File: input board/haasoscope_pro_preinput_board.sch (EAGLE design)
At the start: 20 parts, among them J1 MOLEX_BNC_73100-0105, J4 8pin, K1 AQY21SOP

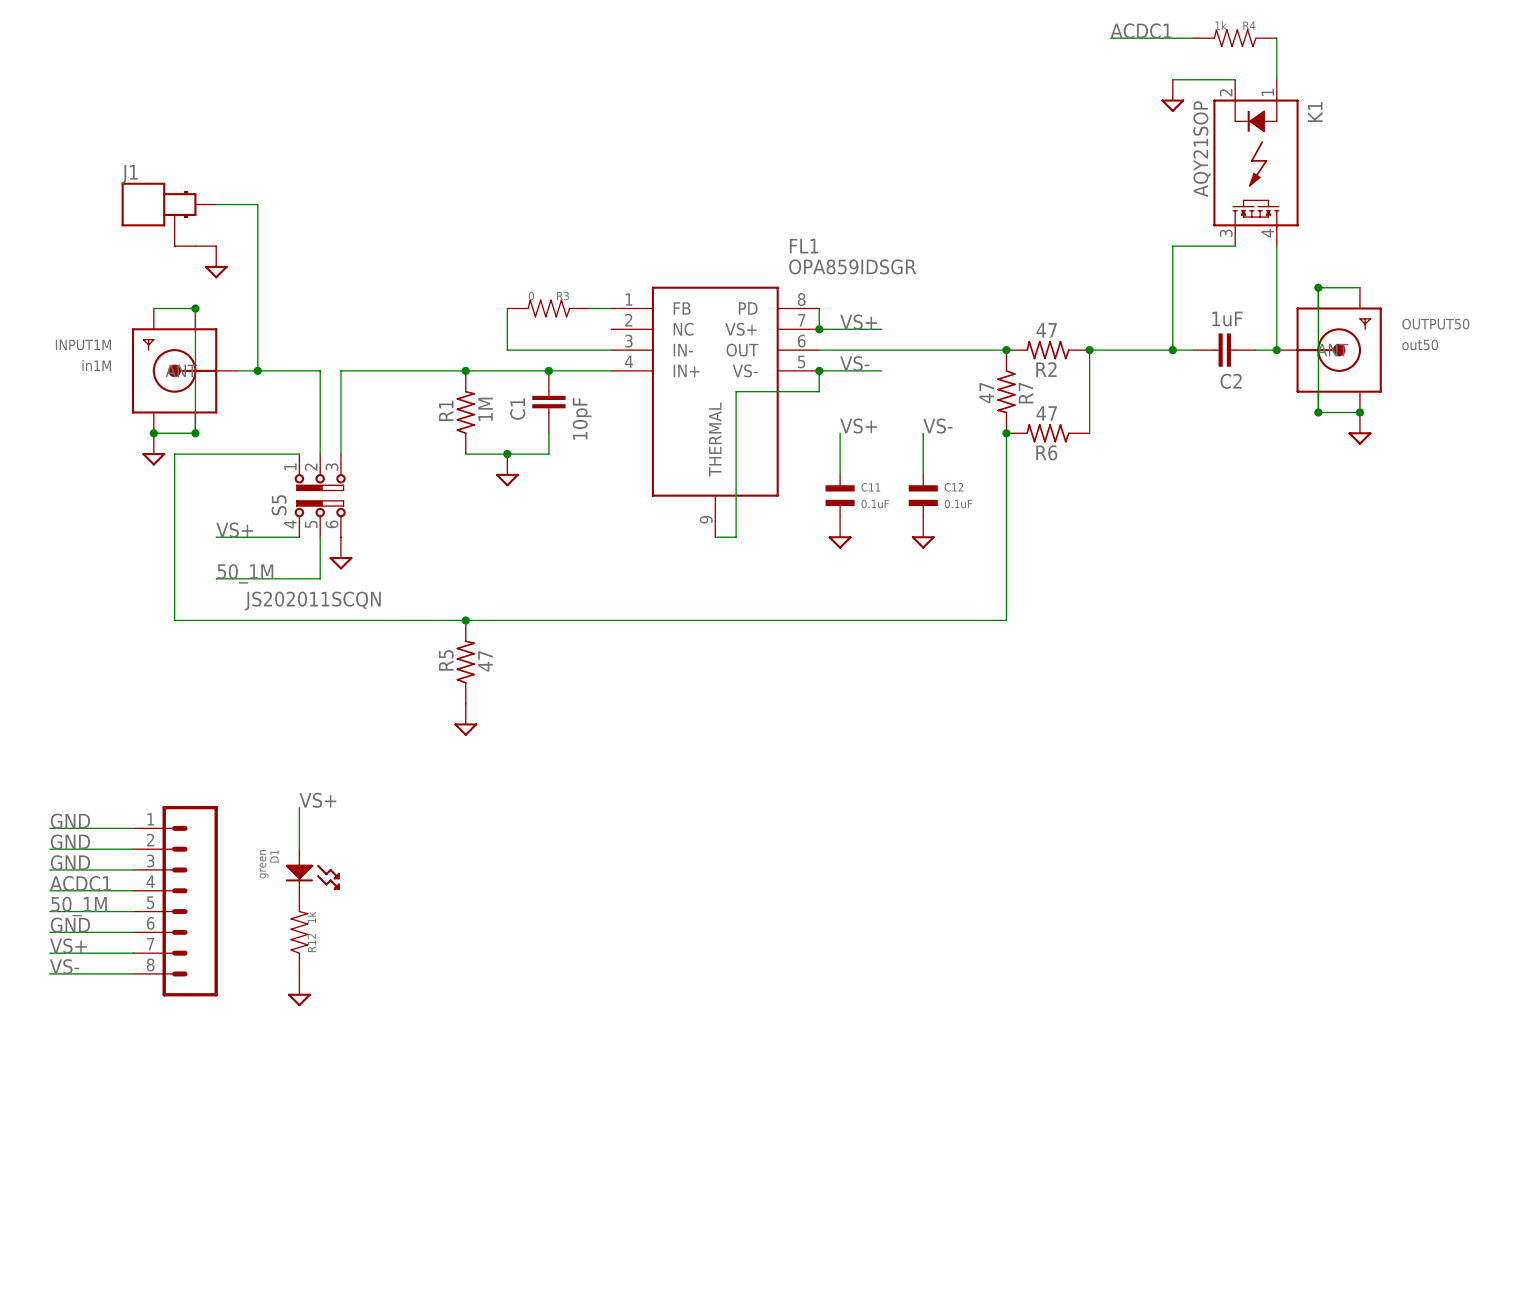
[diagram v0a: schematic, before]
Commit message: use rf relay instead of switch
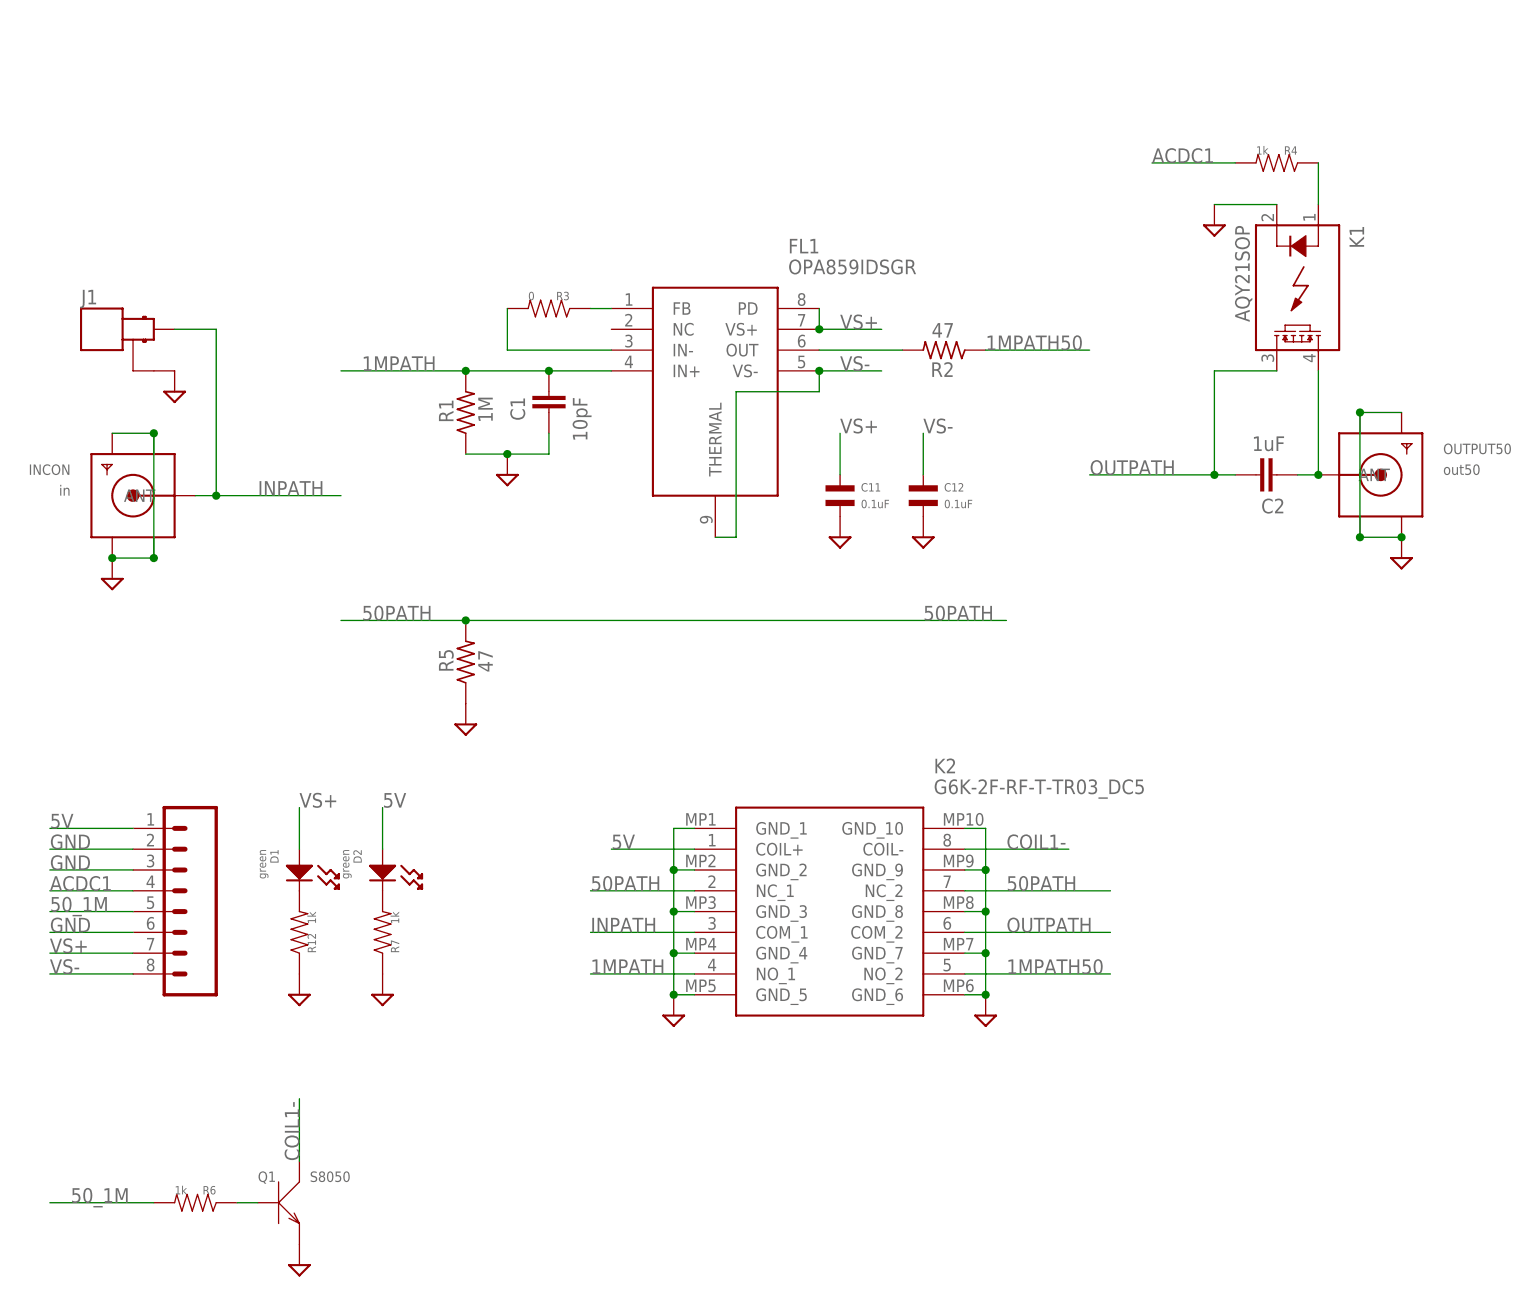
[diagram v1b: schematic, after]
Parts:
- removed INPUT1M: in1M, adafruit:SMACONNECTOR_EDGE
- removed S5: JS202011SCQN, switch-ck:JS202011SCQN
- added D2: green, MF_LEDs:LED_SINGLE-0603
- added INCON: in, adafruit:SMACONNECTOR_EDGE
- added K2: G6K-2F-RF-T-TR03_DC5, G6K-2F-RF-T-TR03_DC5:G6K-2F-RF-T-TR03_DC5
- added Q1: S8050, Seeed-Transistor:SMD-TRANSISTORS-NPN-25V-500MW-S8050(SOT-23)
- K1: LCSC (none) -> C7435105
- R6, R7: value 47 -> 1k; device resistor:R-US_R0805 -> MF_Passives:RESISTOR_0402
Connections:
- removed net N$10: C1.2, FL1.IN+, R1.2, S5.3
- removed net N$13: R5.2, R6.2, R7.2, S5.1
- removed net N$8: C2.2, K1.DS2, R2.1, R6.1
- new net 1MPATH: C1.2, FL1.IN+, K2.NO_1, R1.2
- new net 1MPATH50: K2.NO_2, R2.1
- new net 50PATH: K2.NC_1, K2.NC_2, R5.2
- new net 5V: D2.ANODE, J4.1, K2.COIL+
- new net COIL1-: K2.COIL-, Q1.C
- new net INPATH: INCON.ANT, J1.SIGNAL, K2.COM_1
- new net N$7: D2.CATHODE, R7.P$2
- new net OUTPATH: C2.2, K1.DS2, K2.COM_2
- net 50_1M: now also R6.P$2; no longer S5.5
- net GND: now also INCON.GND1, INCON.GND2, INCON.GND3, INCON.GND4, K2.GND_1, K2.GND_10, K2.GND_2, K2.GND_3, K2.GND_4, K2.GND_5, K2.GND_6, K2.GND_7, K2.GND_8, K2.GND_9, Q1.E, R7.P$1; no longer INPUT1M.GND1, INPUT1M.GND2, INPUT1M.GND3, INPUT1M.GND4, J4.1, S5.6
- net N$4: no longer R7.1
- net N$6: now also Q1.B, R6.P$1; no longer INPUT1M.ANT, J1.SIGNAL, S5.2
- net VS+: no longer S5.4
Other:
- moved on the sheet: C2, J1, K1, OUTPUT50, R2, R4, R6, R7

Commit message: use rf relay instead of switch
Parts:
- K2: LCSC (none) -> C397195
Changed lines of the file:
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@@
 <part name="R5" library="resistor" library_urn="urn:adsk.eagle:library:348" deviceset="R-US_" device="R0805" package3d_urn="urn:adsk.eagle:package:23553/2" value="47"/>
 <part name="SUPPLY5" library="supply2" library_urn="urn:adsk.eagle:library:372" deviceset="GND" device=""/>
-<part name="K2" library="G6K-2F-RF-T-TR03_DC5" deviceset="G6K-2F-RF-T-TR03_DC5" device=""/>
+<part name="K2" library="G6K-2F-RF-T-TR03_DC5" deviceset="G6K-2F-RF-T-TR03_DC5" device="">
+<attribute name="LCSC" value="C397195"/>
+</part>
 <part name="Q1" library="Seeed-Transistor" library_urn="urn:adsk.eagle:library:477" deviceset="SMD-TRANSISTORS-NPN-25V-500MW-S8050(SOT-23)" device="" package3d_urn="urn:adsk.eagle:package:33015/1" value="S8050">
 <attribute name="LCSC" value="C7420370"/>
@@
 <attribute name="NAME" x="306.07" y="25.4" size="1.778" layer="95" align="center-left"/>
 <attribute name="VALUE" x="306.07" y="22.86" size="1.778" layer="96" align="center-left"/>
+<attribute name="LCSC" x="276.86" y="17.78" size="1.778" layer="96" display="off"/>
 </instance>
 <instance part="Q1" gate="G$1" x="226.06" y="-27.94" smashed="yes">

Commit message: add attenuator and fix relay footprint
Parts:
- removed K2: G6K-2F-RF-T-TR03_DC5, G6K-2F-RF-T-TR03_DC5:G6K-2F-RF-T-TR03_DC5
- removed OUTPUT50: out50, adafruit:SMACONNECTOR_EDGE
- removed R3: 0, MF_Passives:RESISTOR_0402
- added K3: G6K-2F-RF-DC3, G6K-2F-RF-DC3:G6K-2F-RF-DC3
- added OUTPUT501, OUTPUT502: out50, adafruit:SMACONNECTOR_EDGE
- added R10, R8, R9: 47, resistor:R-US_R0805
- added R11: 120, resistor:R-US_R0805
- added R13, R14: 75, resistor:R-US_R0805
- D1, D2: LCSC (none) -> C2286
- R5: value 47 -> ?50?
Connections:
- removed net N$2: FL1.IN-, R3.P$2
- removed net N$3: C2.1, K1.DS1, OUTPUT50.ANT
- new net N$10: OUTPUT501.ANT, R10.1, R9.1
- new net N$8: C2.1, K1.DS1, R8.2, R9.2
- new net N$9: OUTPUT502.ANT, R10.2, R8.1
- new net OUTPATHFILT: C2.2, K1.DS2, R11.1, R13.1
- net 1MPATH: now also K3.NO_1; no longer K2.NO_1
- net 1MPATH50: now also K3.NO_2; no longer K2.NO_2
- net 50PATH: now also K3.NC_1, K3.NC_2; no longer K2.NC_1, K2.NC_2
- net 5V: now also K3.COIL+; no longer K2.COIL+
- net COIL1-: now also K3.COIL-; no longer K2.COIL-
- net GND: now also K3.MP1, K3.MP2, OUTPUT501.GND1, OUTPUT501.GND2, OUTPUT501.GND3, OUTPUT501.GND4, OUTPUT502.GND1, OUTPUT502.GND2, OUTPUT502.GND3, OUTPUT502.GND4, R13.2, R14.2; no longer K2.GND_1, K2.GND_10, K2.GND_2, K2.GND_3, K2.GND_4, K2.GND_5, K2.GND_6, K2.GND_7, K2.GND_8, K2.GND_9, OUTPUT50.GND1, OUTPUT50.GND2, OUTPUT50.GND3, OUTPUT50.GND4
- net INPATH: now also K3.COM_1; no longer K2.COM_1
- net N$5: now also FL1.IN-; no longer R3.P$1
- net OUTPATH: now also K3.COM_2, R11.2, R14.1; no longer C2.2, K1.DS2, K2.COM_2
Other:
- note added: "AC/DC coupling"
- note added: "Pi attenuator 1/5, -14dB 50 Ohm"
- note added: "RF relay"
- note added: "RF relay driver"
- moved on the sheet: C2, K1, Q1, R4, R6

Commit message: add relay for attenuator
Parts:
- added K2: G6K-2F-RF-DC3, G6K-2F-RF-DC3:G6K-2F-RF-DC3
- added Q2: S8050, Seeed-Transistor:SMD-TRANSISTORS-NPN-25V-500MW-S8050(SOT-23)
- added R3: 1k, MF_Passives:RESISTOR_0402
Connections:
- new net ATT: J4.3, R3.P$2
- new net COIL2-: K2.COIL-, Q2.C
- new net FILTIN: K2.NO_1, R11.2, R14.1
- new net FILTOUT: K2.NO_2, R11.1, R13.1
- new net N$2: Q2.B, R3.P$1
- new net NOFILT: K2.NC_1, K2.NC_2
- net 5V: now also K2.COIL+
- net GND: now also K2.MP1, K2.MP2, Q2.E; no longer J4.3
- net OUTPATH: now also K2.COM_1; no longer R11.2, R14.1
- net OUTPATHFILT: now also K2.COM_2; no longer R11.1, R13.1
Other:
- note added: "50 Ohm resistive splitter/combiner Output -6dB"
- note added: "RF relay driver for attenuator"
- note added: "RF relay driver for input Z"
- note added: "RF relay for attenuator"
- note added: "RF relay for input Z"
- note removed: "RF relay driver"
- moved on the sheet: C2, K1, OUTPUT501, OUTPUT502, R10, R11, R13, R14, R4, R8, R9

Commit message: don't place 10pF, fix some labels
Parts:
- C1: value 10pF -> ?10pF?
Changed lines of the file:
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@@
 <part name="FL1" library="OPA859IDSGR" deviceset="OPA859IDSGR" device=""/>
 <part name="R1" library="resistor" library_urn="urn:adsk.eagle:library:348" deviceset="R-US_" device="R0805" package3d_urn="urn:adsk.eagle:package:23553/2" value="1M"/>
-<part name="C1" library="resistor" library_urn="urn:adsk.eagle:library:348" deviceset="C-EU" device="C0805" package3d_urn="urn:adsk.eagle:package:23617/2" value="10pF"/>
+<part name="C1" library="resistor" library_urn="urn:adsk.eagle:library:348" deviceset="C-EU" device="C0805" package3d_urn="urn:adsk.eagle:package:23617/2" value="?10pF?"/>
 <part name="SUPPLY1" library="supply2" library_urn="urn:adsk.eagle:library:372" deviceset="GND" device=""/>
 <part name="R2" library="resistor" library_urn="urn:adsk.eagle:library:348" deviceset="R-US_" device="R0805" package3d_urn="urn:adsk.eagle:package:23553/2" value="47"/>

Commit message: add relay for splitter add ethernet jack for testing lvds add connector and trace test lines
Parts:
- removed INCON: in, adafruit:SMACONNECTOR_EDGE
- removed J1: MOLEX_BNC_73100-0105, connector:MOLEX_BNC_73100-0105
- removed OUTPUT501, OUTPUT502: out50, adafruit:SMACONNECTOR_EDGE
- added BNCIN, TESTBNC1, TESTBNC2: MOLEX_BNC_73100-0105, connector:MOLEX_BNC_73100-0105
- added C3: 1uF, MF_Passives:CAPACITOR_NP_0402
- added J2: 8pin, SparkFun-Connectors:CONN_08"
- added K4: G6K-2F-RF-DC3, G6K-2F-RF-DC3:G6K-2F-RF-DC3
- added OUTMAIN, OUTSPLIT, TESTSMA1, TESTSMA2, TESTSMA3, TESTSMA4: out50, adafruit:SMACONNECTOR_EDGE
- added Q3: S8050, Seeed-Transistor:SMD-TRANSISTORS-NPN-25V-500MW-S8050(SOT-23)
- added R15, R16: 75, MF_Passives:RESISTOR_0402
- added U$1: RJ45-CONNECTOR-SHIELDED, FlashPCB_Connectors:RJ45-CONNECTOR-SHIELDED
- C2: device resistor:C-EUC0805 -> MF_Passives:CAPACITOR_NP_0402
- R10, R11, R8, R9: device resistor:R-US_R0805 -> MF_Passives:RESISTOR_0402
- R13: value 75 -> 1k; device resistor:R-US_R0805 -> MF_Passives:RESISTOR_0402; LCSC C113304 -> (none)
- R14: value 75 -> 0; device resistor:R-US_R0805 -> MF_Passives:RESISTOR_0402; LCSC C113304 -> (none)
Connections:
- net 50_1M renamed 50_1M_CONTROL
- net ACDC1 renamed ACDC_CONTROL
- net ATT renamed ATT_CONTROL
- new net COIL3-: K4.COIL-, Q3.C
- new net DA_N: J2.2, U$1.2
- new net DA_P: J2.1, U$1.1
- new net DB_N: J2.4, U$1.6
- new net DB_P: J2.3, U$1.3
- new net DC_N: J2.6, U$1.5
- new net DC_P: J2.5, U$1.4
- new net DD_N: J2.8, U$1.8
- new net DD_P: J2.7, U$1.7
- new net N$12: C3.P$1, R14.P$1
- new net N$13: C3.P$2, TESTSMA4.ANT
- new net N$3: Q3.B, R13.P$1
- new net NOSPLIT: K4.NC_1, K4.NC_2
- new net OUTMAIN: K4.COM_2, OUTMAIN.ANT
- new net OUTPATHACDC: C2.P$2, K1.DS1, K4.COM_1
- new net OUTSPLIT: OUTSPLIT.ANT, R10.P$2, R9.P$2
- new net SPLIT: K4.NO_1, R8.P$1, R9.P$1
- new net SPLITOUT: K4.NO_2, R10.P$1, R8.P$2
- new net SPLIT_CONTROL: J4.6, R13.P$2
- net 5V: now also K4.COIL+
- net FILTIN: now also R11.P$1, R15.P$1; no longer R11.2, R14.1
- net FILTOUT: now also R11.P$2, R16.P$1; no longer R11.1, R13.1
- net GND: now also BNCIN.GND, K4.MP1, K4.MP2, OUTMAIN.GND1, OUTMAIN.GND2, OUTMAIN.GND3, OUTMAIN.GND4, OUTSPLIT.GND1, OUTSPLIT.GND2, OUTSPLIT.GND3, OUTSPLIT.GND4, Q3.E, R15.P$2, R16.P$2, TESTBNC1.GND, TESTBNC2.GND, TESTSMA1.GND1, TESTSMA1.GND2, TESTSMA1.GND3, TESTSMA1.GND4, TESTSMA2.GND1, TESTSMA2.GND2, TESTSMA2.GND3, TESTSMA2.GND4, TESTSMA3.GND1, TESTSMA3.GND2, TESTSMA3.GND3, TESTSMA3.GND4, TESTSMA4.GND1, TESTSMA4.GND2, TESTSMA4.GND3, TESTSMA4.GND4, U$1.SHIELD; no longer INCON.GND1, INCON.GND2, INCON.GND3, INCON.GND4, J1.GND, J4.6, OUTPUT501.GND1, OUTPUT501.GND2, OUTPUT501.GND3, OUTPUT501.GND4, OUTPUT502.GND1, OUTPUT502.GND2, OUTPUT502.GND3, OUTPUT502.GND4, R13.2, R14.2
- net INPATH: now also BNCIN.SIGNAL; no longer INCON.ANT, J1.SIGNAL
- net N$10: now also R14.P$2, TESTSMA3.ANT; no longer OUTPUT501.ANT, R10.1, R9.1
- net N$8: now also TESTBNC1.SIGNAL, TESTBNC2.SIGNAL; no longer C2.1, K1.DS1, R8.2, R9.2
- net N$9: now also TESTSMA1.ANT, TESTSMA2.ANT; no longer OUTPUT502.ANT, R10.2, R8.1
- net OUTPATHFILT: now also C2.P$1; no longer C2.2
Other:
- note added: "RF relay driver for splitting"
- note added: "RF relay for splitting"
- moved on the sheet: D1, D2, K3, Q1, R10, R11, R12, R13, R14, R6, R7, R8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
